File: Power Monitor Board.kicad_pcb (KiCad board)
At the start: 2 copper layers, 13 parts, among them U1 ACS709xLFTR-10BB, U10 ACS709xLFTR-10BB, U11 ACS709xLFTR-10BB, U12 ACS709xLFTR-10BB, U2 ACS709xLFTR-10BB, U3 ACS709xLFTR-10BB, U4 ACS709xLFTR-10BB, U5 ACS709xLFTR-10BB, U6 ACS709xLFTR-10BB, U7 ACS709xLFTR-10BB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

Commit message: Add files via upload
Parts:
- removed U10, U11, U12, U9: ACS709xLFTR-10BB, Sensor_Current:Allegro_QSOP-24_3.9x8.7mm_P0.635mm
- added J1: Conn_01x02_Socket, Connector:Banana_Jack_2Pin, F.Cu at (99.5, 29.0)
- added J10: Conn_01x02_Pin, Connector_AMASS:AMASS_XT60-M_1x02_P7.20mm_Vertical, F.Cu at (115.6, 102.9)
- added J11: Conn_01x02_Pin, Connector_AMASS:AMASS_XT60-M_1x02_P7.20mm_Vertical, F.Cu at (115.6, 113.2)
- added J2: Conn_01x02_Pin, Connector_AMASS:AMASS_XT60-M_1x02_P7.20mm_Vertical, F.Cu at (115.5, 41.5)
- added J3: Conn_01x01_Socket, Connector_PinSocket_2.54mm:PinSocket_1x01_P2.54mm_Vertical, F.Cu at (140.0, 25.5)
- added J4: Conn_01x01_Socket, Connector_PinSocket_2.54mm:PinSocket_1x01_P2.54mm_Vertical, F.Cu at (140.0, 31.5)
- added J5: Conn_01x02_Pin, Connector_AMASS:AMASS_XT60-M_1x02_P7.20mm_Vertical, F.Cu at (115.6, 51.7)
- added J6: Conn_01x02_Pin, Connector_AMASS:AMASS_XT60-M_1x02_P7.20mm_Vertical, F.Cu at (115.6, 61.9)
- added J7: Conn_01x02_Pin, Connector_AMASS:AMASS_XT60-M_1x02_P7.20mm_Vertical, F.Cu at (115.6, 72.2)
- added J8: Conn_01x02_Pin, Connector_AMASS:AMASS_XT60-M_1x02_P7.20mm_Vertical, F.Cu at (115.6, 82.4)
- added J9: Conn_01x02_Pin, Connector_AMASS:AMASS_XT60-M_1x02_P7.20mm_Vertical, F.Cu at (115.6, 92.7)
- U1, U2, U3, U4, U5, U6, U7, U8: value ACS709xLFTR-10BB -> ACS711xLCTR-25AB; footprint Sensor_Current:Allegro_QSOP-24_3.9x8.7mm_P0.635mm -> Package_SO:SOIC-8_3.9x4.9mm_P1.27mm
- moved U1 26.8 mm to (136.4, 53.0)
- moved U4 22.5 mm to (136.5, 72.8)
- moved U7 21.9 mm to (136.5, 92.6)
- moved U8 16.2 mm to (136.5, 99.1)
- moved U2 15.7 mm to (136.5, 59.7)
- moved U5 12.8 mm to (136.5, 79.4)
- moved U6 8.02 mm to (136.5, 86.0)
- moved U3 4.71 mm to (136.5, 66.2)
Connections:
- A2 pad A0: Net-(U1-VIOUT) -> Arduino Mega A0
- A2 pad A1: Net-(U2-VIOUT) -> Arduino Mega A1
- A2 pad A10: Net-(U11-VIOUT) -> unconnected-(A2-PadA10)
- A2 pad A11: Net-(U12-VIOUT) -> unconnected-(A2-PadA11)
- A2 pad A2: Net-(U3-VIOUT) -> Arduino Mega A2
- A2 pad A3: Net-(U4-VIOUT) -> Arduino Mega A3
- A2 pad A4: Net-(U5-VIOUT) -> Arduino Mega A4
- A2 pad A5: Net-(U6-VIOUT) -> Arduino Mega A5
- A2 pad A6: Net-(U7-VIOUT) -> Arduino Mega A6
- A2 pad A7: Net-(U8-VIOUT) -> Arduino Mega A7
- A2 pad A8: Net-(U9-VIOUT) -> unconnected-(A2-PadA8)
- A2 pad A9: Net-(U10-VIOUT) -> unconnected-(A2-PadA9)
- A2 pad VIN: +5V -> 5V VCC
- U1 pad 1: Channel1IN -> Power Supply +
- U1 pad 2: Channel1IN -> Power Supply +
- U1 pad 3: Channel1IN -> Motor 1 +
- U1 pad 4: Channel1IN -> Motor 1 +
- U1 pad 5: Channel1IN -> GND
- U1 pad 6: Channel1IN -> unconnected-(U1-~{FAULT}-Pad6)
- U1 pad 7: Net-(U1-IP--Pad10) -> Arduino Mega A0
- U1 pad 8: Net-(U1-IP--Pad10) -> 5V VCC
- U2 pad 1: Channel2IN -> Power Supply +
- U2 pad 2: Channel2IN -> Power Supply +
- U2 pad 3: Channel2IN -> Motor 2 +
- U2 pad 4: Channel2IN -> Motor 2 +
- U2 pad 5: Channel2IN -> GND
- U2 pad 6: Channel2IN -> unconnected-(U2-~{FAULT}-Pad6)
- U2 pad 7: Net-(U2-IP--Pad10) -> Arduino Mega A1
- U2 pad 8: Net-(U2-IP--Pad10) -> 5V VCC
- U3 pad 1: Channel3IN -> Power Supply +
- U3 pad 2: Channel3IN -> Power Supply +
- U3 pad 3: Channel3IN -> Motor 3 +
- U3 pad 4: Channel3IN -> Motor 3 +
- U3 pad 5: Channel3IN -> GND
- U3 pad 6: Channel3IN -> unconnected-(U3-~{FAULT}-Pad6)
- U3 pad 7: Net-(U3-IP--Pad10) -> Arduino Mega A2
- U3 pad 8: Net-(U3-IP--Pad10) -> 5V VCC
- U4 pad 1: Channel4IN -> Power Supply +
- U4 pad 2: Channel4IN -> Power Supply +
- U4 pad 3: Channel4IN -> Motor 4 +
- U4 pad 4: Channel4IN -> Motor 4 +
- U4 pad 5: Channel4IN -> GND
- U4 pad 6: Channel4IN -> unconnected-(U4-~{FAULT}-Pad6)
- U4 pad 7: Net-(U4-IP--Pad10) -> Arduino Mega A3
- U4 pad 8: Net-(U4-IP--Pad10) -> 5V VCC
- U5 pad 1: Channel5IN -> Power Supply +
- U5 pad 2: Channel5IN -> Power Supply +
- U5 pad 3: Channel5IN -> Motor 5 +
- U5 pad 4: Channel5IN -> Motor 5 +
- U5 pad 5: Channel5IN -> GND
- U5 pad 6: Channel5IN -> unconnected-(U5-~{FAULT}-Pad6)
- U5 pad 7: Net-(U5-IP--Pad10) -> Arduino Mega A4
- U5 pad 8: Net-(U5-IP--Pad10) -> 5V VCC
- U6 pad 1: Channel6IN -> Power Supply +
- U6 pad 2: Channel6IN -> Power Supply +
- U6 pad 3: Channel6IN -> Motor 6 +
- U6 pad 4: Channel6IN -> Motor 6 +
- U6 pad 5: Channel6IN -> GND
- U6 pad 6: Channel6IN -> unconnected-(U6-~{FAULT}-Pad6)
- U6 pad 7: Net-(U6-IP--Pad10) -> Arduino Mega A5
- U6 pad 8: Net-(U6-IP--Pad10) -> 5V VCC
- U7 pad 1: Channel7IN -> Power Supply +
- U7 pad 2: Channel7IN -> Power Supply +
- U7 pad 3: Channel7IN -> Motor 7 +
- U7 pad 4: Channel7IN -> Motor 7 +
- U7 pad 5: Channel7IN -> GND
- U7 pad 6: Channel7IN -> unconnected-(U7-~{FAULT}-Pad6)
- U7 pad 7: Net-(U7-IP--Pad10) -> Arduino Mega A6
- U7 pad 8: Net-(U7-IP--Pad10) -> 5V VCC
- U8 pad 1: Channel8IN -> Power Supply +
- U8 pad 2: Channel8IN -> Power Supply +
- U8 pad 3: Channel8IN -> Motor 8 +
- U8 pad 4: Channel8IN -> Motor 8 +
- U8 pad 5: Channel8IN -> GND
- U8 pad 6: Channel8IN -> unconnected-(U8-~{FAULT}-Pad6)
- U8 pad 7: Net-(U8-IP--Pad10) -> Arduino Mega A7
- U8 pad 8: Net-(U8-IP--Pad10) -> 5V VCC
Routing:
- net GND: track 0.00 -> 211.2 mm
- net Power Supply +: track 0.00 -> 113.9 mm
- net 5V VCC: track 0.00 -> 91.7 mm
- net Motor 1 +: track 0.00 -> 23.5 mm
- net Motor 8 +: track 0.00 -> 23.4 mm
- net Motor 7 +: track 0.00 -> 21.9 mm
- net Motor 2 +: track 0.00 -> 21.8 mm
- net Motor 6 +: track 0.00 -> 20.3 mm
- net Motor 3 +: track 0.00 -> 20.3 mm
- net Motor 5 +: track 0.00 -> 18.8 mm
- net Motor 4 +: track 0.00 -> 18.7 mm

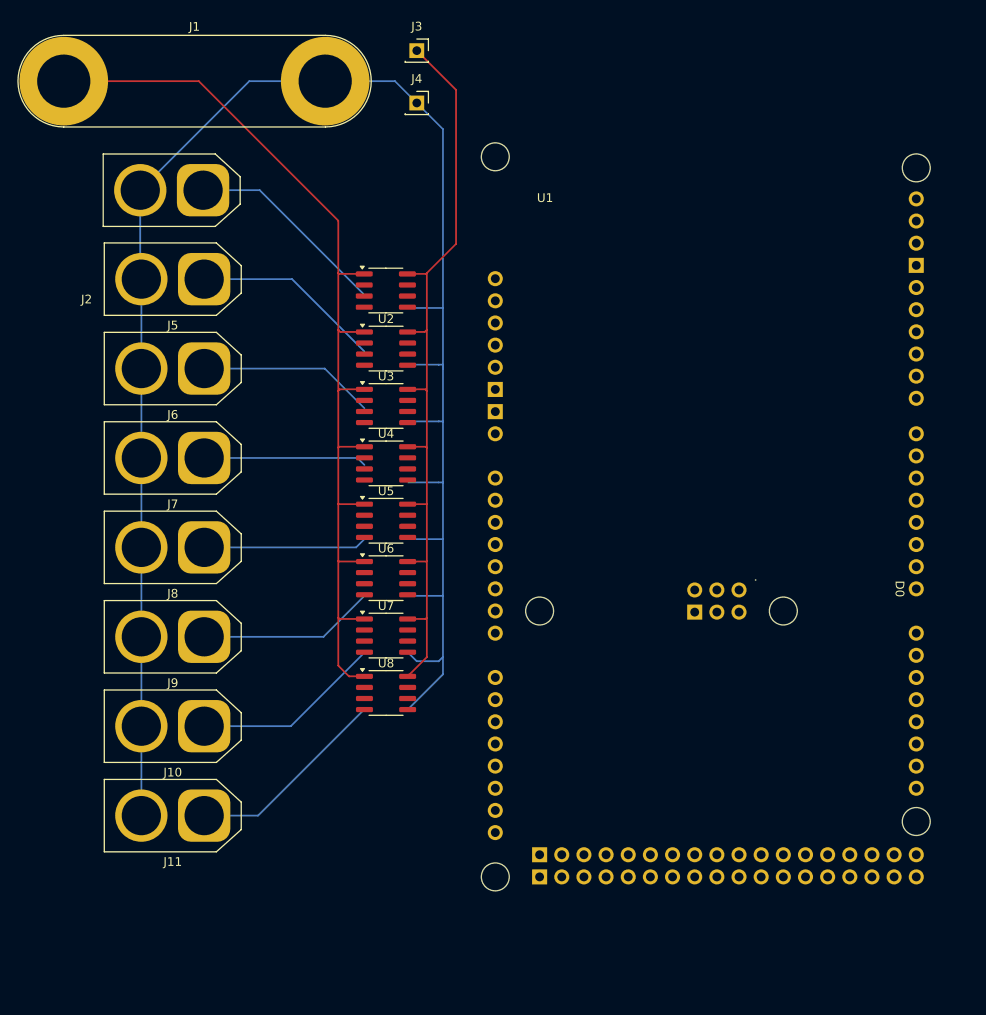
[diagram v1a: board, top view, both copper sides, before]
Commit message: Cleaned up schematic and started layout
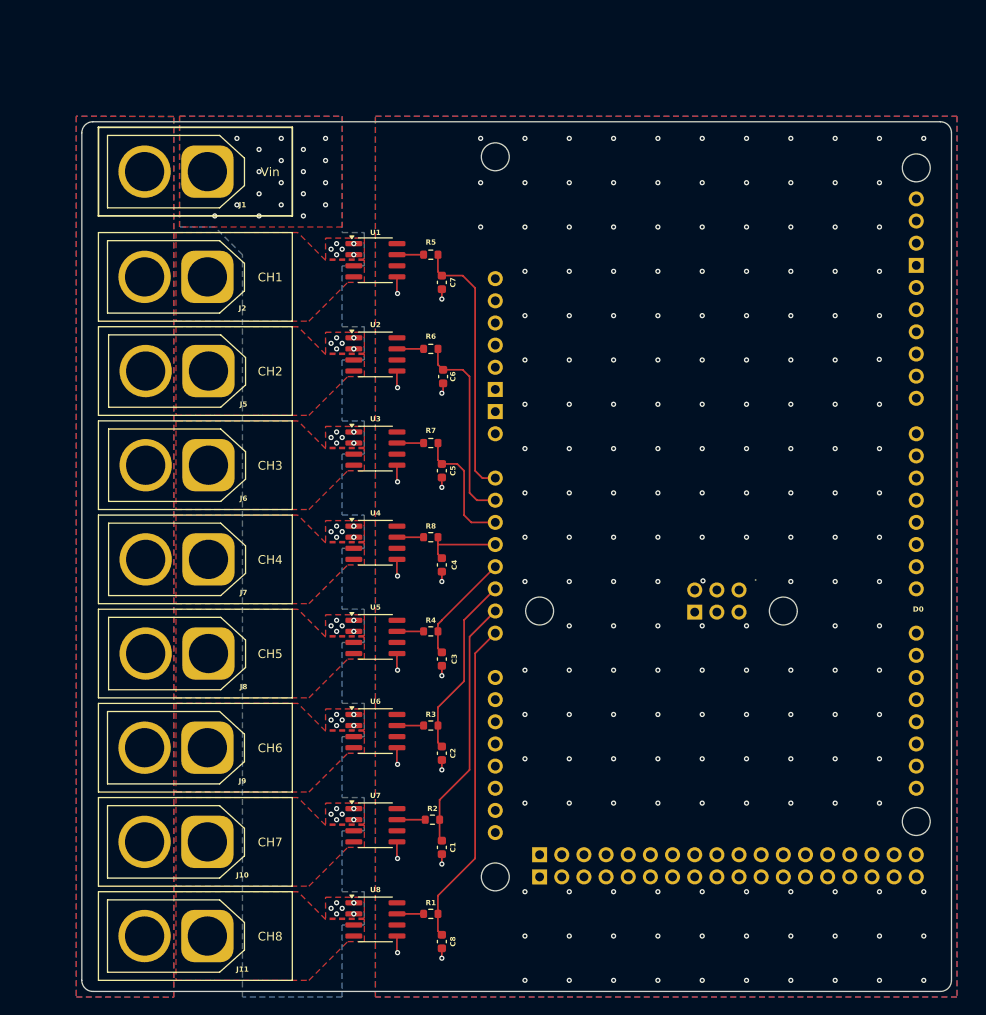
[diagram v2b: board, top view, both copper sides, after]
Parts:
- removed J3, J4: Conn_01x01_Socket, Connector_PinSocket_2.54mm:PinSocket_1x01_P2.54mm_Vertical
- added C1: 0.1u, Capacitor_SMD:C_0603_1608Metric, F.Cu at (142.9, 116.8)
- added C2: 0.1u, Capacitor_SMD:C_0603_1608Metric, F.Cu at (142.9, 106.0)
- added C3: 0.1u, Capacitor_SMD:C_0603_1608Metric, F.Cu at (142.9, 95.2)
- added C4: 0.1u, Capacitor_SMD:C_0603_1608Metric, F.Cu at (142.9, 84.5)
- added C5: 0.1u, Capacitor_SMD:C_0603_1608Metric, F.Cu at (142.9, 73.7)
- added C6: 0.1u, Capacitor_SMD:C_0603_1608Metric, F.Cu at (143.0, 62.9)
- added C7: 0.1u, Capacitor_SMD:C_0603_1608Metric, F.Cu at (142.9, 52.1)
- added C8: 0.1u, Capacitor_SMD:C_0603_1608Metric, F.Cu at (142.9, 127.6)
- added R1: 100R, Resistor_SMD:R_0603_1608Metric, F.Cu at (141.6, 124.5)
- added R2: 100R, Resistor_SMD:R_0603_1608Metric, F.Cu at (141.8, 113.7)
- added R3: 100R, Resistor_SMD:R_0603_1608Metric, F.Cu at (141.6, 102.9)
- added R4: 100R, Resistor_SMD:R_0603_1608Metric, F.Cu at (141.6, 92.1)
- added R5: 100R, Resistor_SMD:R_0603_1608Metric, F.Cu at (141.6, 48.9)
- added R6: 100R, Resistor_SMD:R_0603_1608Metric, F.Cu at (141.6, 59.7)
- added R7: 100R, Resistor_SMD:R_0603_1608Metric, F.Cu at (141.6, 70.5)
- added R8: 100R, Resistor_SMD:R_0603_1608Metric, F.Cu at (141.6, 81.3)
- J1: value Conn_01x02_Socket -> Conn_01x02_Pin; footprint Connector:Banana_Jack_2Pin -> Connector_AMASS:AMASS_XT60-M_1x02_P7.20mm_Vertical
- moved U8 26.0 mm to (135.3, 125.1)
- moved U7 21.8 mm to (135.3, 114.3)
- moved J1 19.5 mm to (116.0, 39.4), turned to 180 degrees
- moved U6 17.6 mm to (135.3, 103.5)
- moved J11 13.8 mm to (116.0, 127.0)
- moved U5 13.4 mm to (135.3, 92.7)
- moved J10 13.3 mm to (116.0, 116.2)
- moved J9 12.7 mm to (116.0, 105.4)
- moved J8 12.2 mm to (116.1, 94.6)
- moved J7 11.6 mm to (116.1, 83.8)
- moved J6 11.1 mm to (116.1, 73.0)
- moved J5 10.5 mm to (116.1, 62.2)
- moved J2 9.95 mm to (116.0, 51.4)
- moved U4 9.18 mm to (135.3, 81.9)
- moved U3 5.04 mm to (135.3, 71.1)
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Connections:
- A2 pad 5V1: unconnected-(A2-5V-Pad5V1) -> +5V
- A2 pad 5V3: unconnected-(A2-5V-Pad5V3) -> +5V
- A2 pad 5V4: unconnected-(A2-5V-Pad5V4) -> +5V
- A2 pad GND2: unconnected-(A2-GND-PadGND2) -> GND
- A2 pad GND3: unconnected-(A2-GND-PadGND3) -> GND
- A2 pad GND5: unconnected-(A2-GND-PadGND5) -> GND
- A2 pad GND6: unconnected-(A2-GND-PadGND6) -> GND
- A2 pad VIN: 5V VCC -> unconnected-(A2-PadVIN)
- J1 pad 2: GND -> Power Supply -
- J10 pad 2: GND -> Power Supply -
- J11 pad 2: GND -> Power Supply -
- J2 pad 2: GND -> Power Supply -
- J5 pad 2: GND -> Power Supply -
- J6 pad 2: GND -> Power Supply -
- J7 pad 2: GND -> Power Supply -
- J8 pad 2: GND -> Power Supply -
- J9 pad 2: GND -> Power Supply -
- U1 pad 7: Arduino Mega A0 -> Net-(U1-VIOUT)
- U1 pad 8: 5V VCC -> +5V
- U2 pad 7: Arduino Mega A1 -> Net-(U2-VIOUT)
- U2 pad 8: 5V VCC -> +5V
- U3 pad 7: Arduino Mega A2 -> Net-(U3-VIOUT)
- U3 pad 8: 5V VCC -> +5V
- U4 pad 7: Arduino Mega A3 -> Net-(U4-VIOUT)
- U4 pad 8: 5V VCC -> +5V
- U5 pad 7: Arduino Mega A4 -> Net-(U5-VIOUT)
- U5 pad 8: 5V VCC -> +5V
- U6 pad 7: Arduino Mega A5 -> Net-(U6-VIOUT)
- U6 pad 8: 5V VCC -> +5V
- U7 pad 7: Arduino Mega A6 -> Net-(U7-VIOUT)
- U7 pad 8: 5V VCC -> +5V
- U8 pad 7: Arduino Mega A7 -> Net-(U8-VIOUT)
- U8 pad 8: 5V VCC -> +5V
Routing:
- net GND: track 211.2 -> 24.6 mm, vias 0 -> 104
- net Power Supply +: track 113.9 -> 0.00 mm, vias 0 -> 67
- net 5V VCC: track 91.7 -> 0.00 mm
- net Arduino Mega A7: track 0.00 -> 37.5 mm
- net Arduino Mega A0: track 0.00 -> 30.6 mm
- net Arduino Mega A6: track 0.00 -> 29.1 mm
- net Motor 1 +: track 23.5 -> 0.00 mm
- net Motor 8 +: track 23.4 -> 0.00 mm
- net Arduino Mega A1: track 0.00 -> 22.6 mm
- net Motor 7 +: track 21.9 -> 0.00 mm
- net Motor 2 +: track 21.8 -> 0.00 mm
- net Arduino Mega A5: track 0.00 -> 21.0 mm
- net Motor 6 +: track 20.3 -> 0.00 mm
- net Motor 3 +: track 20.3 -> 0.00 mm
- net Motor 5 +: track 18.8 -> 0.00 mm
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- added copper zone on F.Cu, net +5V
- added copper zone on B.Cu, net GND
- added copper zone on F.Cu, net Motor 1 +
- added copper zone on F.Cu, net Motor 2 +
- added copper zone on F.Cu, net Motor 3 +
- added copper zone on F.Cu, net Motor 4 +
- added copper zone on F.Cu, net Motor 5 +
- added copper zone on F.Cu, net Motor 6 +
- added copper zone on F.Cu, net Motor 7 +
- added copper zone on F.Cu, net Motor 8 +
- added copper zone on B.Cu, net Power Supply +
- added copper zone on F.Cu, net Power Supply +
- added copper zone on B.Cu, net Power Supply -
- added copper zone on F.Cu, net Power Supply -
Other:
- board outline added: 99.7 x 99.7 mm
- board text added: "CH1"
- board text added: "CH2"
- board text added: "CH3"
- board text added: "CH4"
- board text added: "CH5"
- board text added: "CH6"
- board text added: "CH7"
- board text added: "CH8"
- board text added: "Vin"

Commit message: Add files via upload
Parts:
- added C10: 0.1u, Capacitor_SMD:C_0603_1608Metric, F.Cu at (138.5, 56.5)
- added C11: 0.1u, Capacitor_SMD:C_0603_1608Metric, F.Cu at (138.5, 67.3)
- added C12: 0.1u, Capacitor_SMD:C_0603_1608Metric, F.Cu at (138.5, 78.1)
- added C13: 0.1u, Capacitor_SMD:C_0603_1608Metric, F.Cu at (138.5, 88.9)
- added C14: 0.1u, Capacitor_SMD:C_0603_1608Metric, F.Cu at (138.5, 99.7)
- added C15: 0.1u, Capacitor_SMD:C_0603_1608Metric, F.Cu at (138.5, 110.5)
- added C16: 0.1u, Capacitor_SMD:C_0603_1608Metric, F.Cu at (138.5, 121.3)
- added C17: 0.1u, Capacitor_SMD:C_0603_1608Metric, F.Cu at (145.0, 45.3)
- added C9: 0.1u, Capacitor_SMD:C_0603_1608Metric, F.Cu at (138.5, 45.7)
- added NT1: NetTie_2, NetTie:NetTie-2_SMD_Pad0.5mm, B.Cu at (133.0, 34.5)
- added R10: R, Resistor_THT:R_Axial_DIN0309_L9.0mm_D3.2mm_P12.70mm_Horizontal, F.Cu at (143.7, 36.5)
- added R11: 100R, Resistor_SMD:R_0603_1608Metric, F.Cu at (142.5, 44.0)
- added R9: R, Resistor_THT:R_Axial_DIN0309_L9.0mm_D3.2mm_P12.70mm_Horizontal, F.Cu at (143.7, 40.5)
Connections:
- A2 pad A8: unconnected-(A2-PadA8) -> Arduino Mega A8
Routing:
- net Arduino Mega A8: track 0.00 -> 63.7 mm, vias 0 -> 4
- net Net-(R10-Pad1): track 0.00 -> 27.7 mm
- net Power Supply -: track 0.00 -> 21.0 mm
- net GND: track 24.6 -> 45.3 mm, vias 104 -> 113
- net Power Supply +: track 0.00 -> 13.5 mm
- net +5V: track 0.00 -> 8.06 mm, vias 87 -> 89

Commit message: Add files via upload
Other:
- board text added: "Sunny Zhang 2024/03/21 Arm Power Monitoring Board"
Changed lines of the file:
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@@
+		)
+	)
+	(gr_text "Sunny Zhang\n2024/03/21\nArm Power Monitoring Board"
+		(at 177 130.92 0)
+		(layer "F.SilkS")
+		(effects
+			(font
+				(size 1 1)
+				(thickness 0.15)
+			)
+			(justify left bottom)
 		)
 	)
@@
 	)
 	(via
-		(at 172.72 132.08)
+		(at 191.5 131.5)
 		(size 0.6)
 		(drill 0.3)
@@
 	)
 	(via
-		(at 167.64 132.08)
+		(at 186.42 131.5)
 		(size 0.6)
 		(drill 0.3)
@@
 	)
 	(via
-		(at 177.8 132.08)
-		(size 0.6)
-		(drill 0.3)
+		(at 196.58 131.5)
+		(size 0.6)
+		(drill 0.3)
